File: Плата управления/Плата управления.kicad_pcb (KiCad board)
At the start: 2 copper layers, 66 x 58.4 mm, 113 parts, among them J1 Conn_01x10, J10 Conn_01x02, J11 Conn_01x03, J2 Conn_01x10, J3 Conn_01x02, J4 A, J5 B, J6 C, J7 Conn_01x02, J8 Conn_01x02, J9 Conn_01x02, U1 AT25xxx, U2 LMV7239M5, U3 LMV324, U4 STM32F767VITx, U5 INA283, Y1 8M

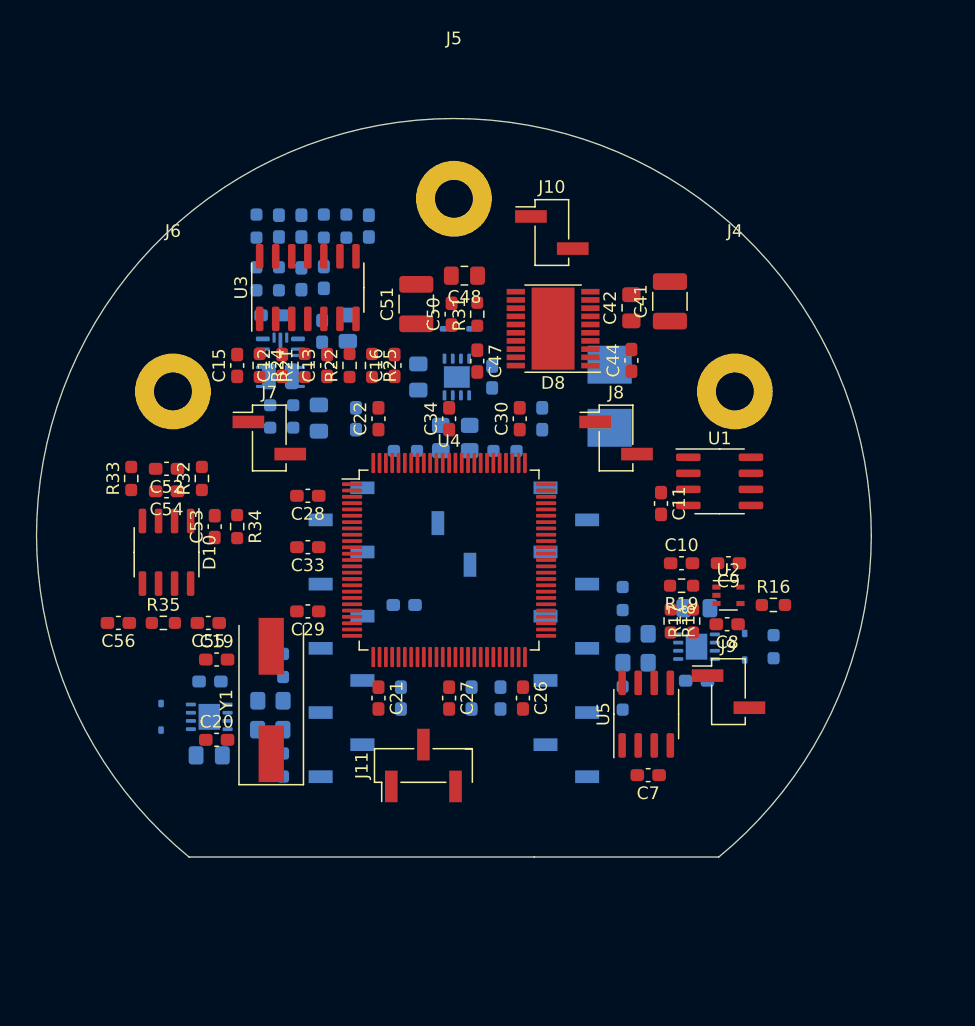
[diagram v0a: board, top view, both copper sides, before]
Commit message: Изменил контур под новую крышку
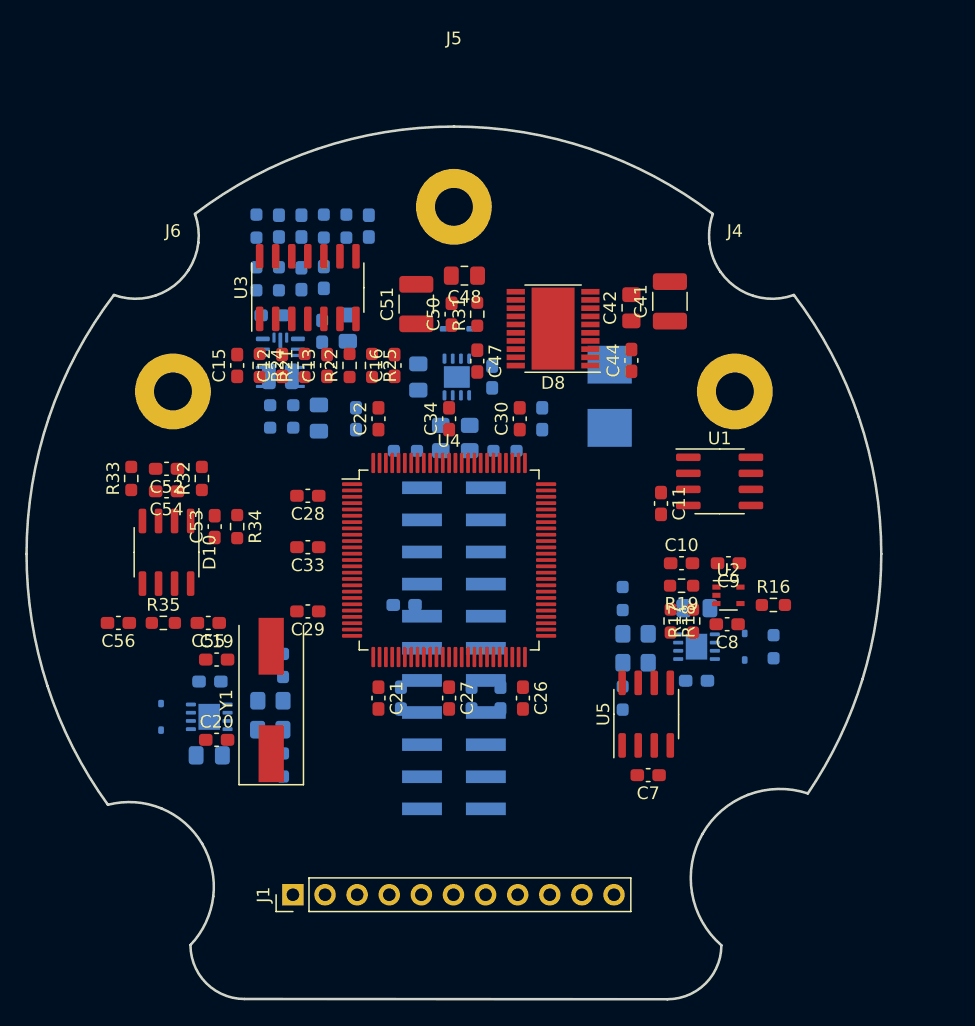
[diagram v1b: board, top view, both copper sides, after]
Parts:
- removed J10, J7, J8, J9: Conn_01x02, Connector_PinHeader_2.54mm:PinHeader_1x02_P2.54mm_Vertical_SMD_Pin1Left
- removed J11: Conn_01x03, Connector_PinHeader_2.54mm:PinHeader_1x03_P2.54mm_Vertical_SMD_Pin1Left
- removed J2: Conn_01x10, Connector_PinSocket_2.54mm:PinSocket_1x10_P2.54mm_Vertical_SMD_Pin1Right
- removed J3: Conn_01x02, Connector_PinSocket_2.54mm:PinSocket_1x02_P2.54mm_Vertical_SMD_Pin1Left
- added J12: Conn_02x11_Odd_Even, Connector_PinHeader_2.54mm:PinHeader_2x11_P2.54mm_Vertical_SMD, B.Cu at (83.2, 103.5)
- J1: value Conn_01x10 -> Conn_01x11; footprint Connector_PinSocket_2.54mm:PinSocket_1x10_P2.54mm_Vertical_SMD_Pin1Left -> Connector_PinHeader_2.54mm:PinHeader_1x11_P2.54mm_Vertical; moved to F.Cu
- moved J1 21.1 mm to (70.5, 123.0), turned to 90 degrees
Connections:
- J1 pad 1: Temp_B -> GND
- J1 pad 10: G5 -> GND
- J1 pad 2: GND -> Current_C_MCU
- J1 pad 4: G4 -> +3.3V
- J1 pad 5: GND -> SCLK_MCU
- J1 pad 6: G6 -> CS_MCU
- J1 pad 7: Temp_C -> SDIO_MCU
- J1 pad 9: C -> Current_B_MCU
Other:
- board size 66 x 58.4 mm -> 67.6 x 69 mm

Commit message: Добавил разъёмы под интерфейсы
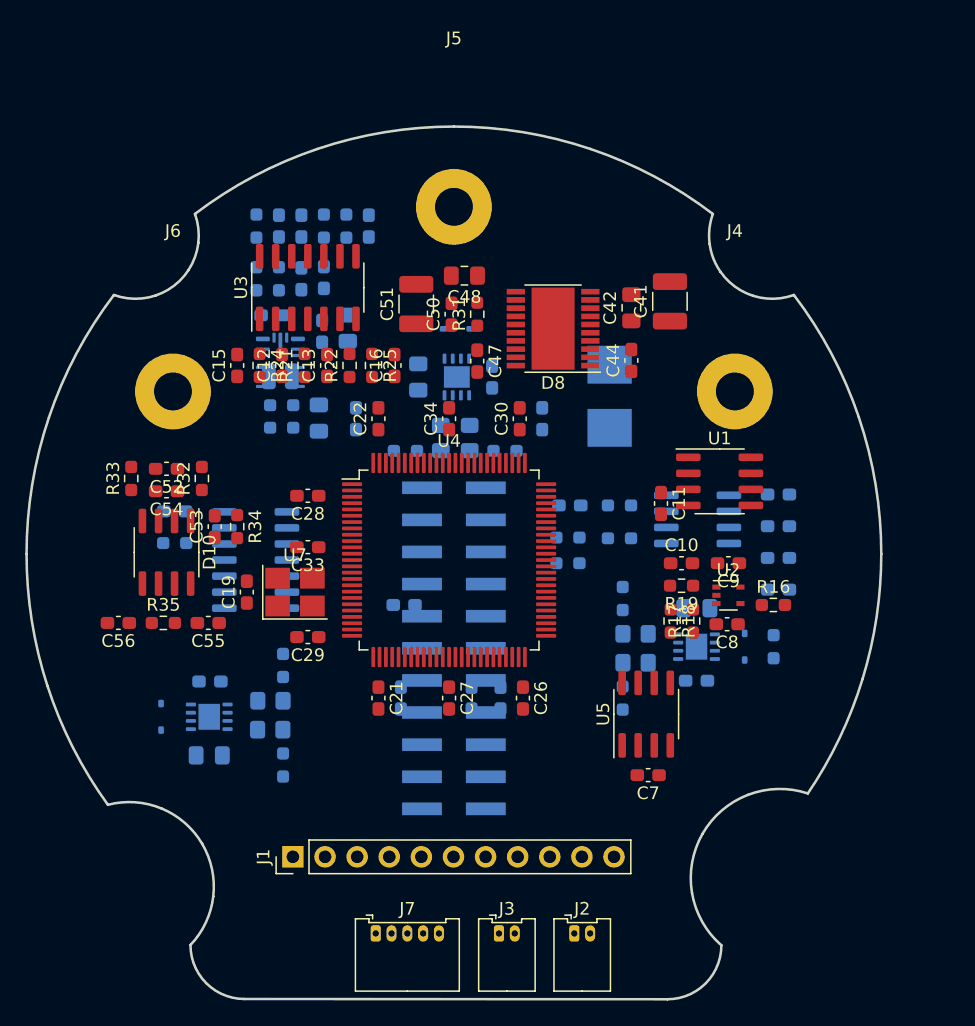
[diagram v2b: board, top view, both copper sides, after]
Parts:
- removed C20: 4.3p, Capacitor_SMD:C_0603_1608Metric_Pad1.08x0.95mm_HandSolder
- removed Y1: 8M, Crystal:Crystal_SMD_HC49-SD
- added C38: 1u, Capacitor_SMD:C_0603_1608Metric_Pad1.08x0.95mm_HandSolder, B.Cu at (108.9, 91.3)
- added C39: 56p, Capacitor_SMD:C_0603_1608Metric_Pad1.08x0.95mm_HandSolder, B.Cu at (108.9, 93.8)
- added C40: 1u, Capacitor_SMD:C_0603_1608Metric_Pad1.08x0.95mm_HandSolder, B.Cu at (108.9, 96.4)
- added C57: 56p, Capacitor_SMD:C_0603_1608Metric_Pad1.08x0.95mm_HandSolder, B.Cu at (108.9, 98.9)
- added C58: 56p, Capacitor_SMD:C_0603_1608Metric_Pad1.08x0.95mm_HandSolder, B.Cu at (92.4, 92.2)
- added C59: 0.1u, Capacitor_SMD:C_0603_1608Metric_Pad1.08x0.95mm_HandSolder, B.Cu at (61.1, 92.7)
- added D7: SIT65HVD232DR, Package_SO:SOIC-8_3.9x4.9mm_P1.27mm, B.Cu at (102.5, 93.3)
- added J2: CAN2, Connector_Molex:Molex_PicoBlade_53048-0210_1x02_P1.25mm_Horizontal, F.Cu at (92.7, 126.1)
- added J3: CAN1, Connector_Molex:Molex_PicoBlade_53048-0210_1x02_P1.25mm_Horizontal, F.Cu at (86.8, 126.1)
- added J7: RS485, Connector_Molex:Molex_PicoBlade_53048-0510_1x05_P1.25mm_Horizontal, F.Cu at (77.0, 126.1)
- added R27: 10k, Resistor_SMD:R_0603_1608Metric_Pad0.98x0.95mm_HandSolder, B.Cu at (96.3, 92.2)
- added R28: 10k, Resistor_SMD:R_0603_1608Metric_Pad0.98x0.95mm_HandSolder, B.Cu at (96.3, 94.8)
- added R36: 10k, Resistor_SMD:R_0603_1608Metric_Pad0.98x0.95mm_HandSolder, B.Cu at (92.2, 94.7)
- added R37: 120, Resistor_SMD:R_0603_1608Metric_Pad0.98x0.95mm_HandSolder, B.Cu at (92.2, 96.8)
- added R38: 120, Resistor_SMD:R_0603_1608Metric_Pad0.98x0.95mm_HandSolder, B.Cu at (61.1, 95.2)
- added U6: ADM3491ExR, Package_SO:SOIC-14_3.9x8.7mm_P1.27mm, B.Cu at (67.5, 96.5)
- added U7: ASEMB-10, Oscillator:Oscillator_SMD_Abracon_ASE-4Pin_3.2x2.5mm_HandSoldering, F.Cu at (70.6, 99.1)
- C19: value 4.3p -> 0.1u
- C52, C54: value 56p -> 1u
- moved C19 5.84 mm to (66.8, 99.1), turned to 90 degrees
- moved J1 3.00 mm to (70.5, 120.0)
- moved C29 2.03 mm to (71.6, 102.6)
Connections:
- net CANH renamed CAN1H
- net CANL renamed CAN1L
- net CAN_RXD renamed CAN1_RXD_MCU
- net CAN_TXD renamed CAN1_TXD_MCU
- C19 pad 2: Net-(U4-PH0) -> +3.3V
- U4 pad 13: Net-(U4-PH1) -> GND

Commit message: Новый контур платы
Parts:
- removed R34, R36: 10k, Resistor_SMD:R_0603_1608Metric_Pad0.98x0.95mm_HandSolder
- added C20: 56p, Capacitor_SMD:C_0603_1608Metric_Pad1.08x0.95mm_HandSolder, B.Cu at (105.7, 98.0)
- added C60: 56p, Capacitor_SMD:C_0603_1608Metric_Pad1.08x0.95mm_HandSolder, B.Cu at (108.2, 98.0)
- added C61: 56p, Capacitor_SMD:C_0603_1608Metric_Pad1.08x0.95mm_HandSolder, B.Cu at (103.6, 94.0)
- added J10: Conn_02x03_Odd_Even, Connector_PinHeader_2.54mm:PinHeader_2x03_P2.54mm_Vertical_SMD, F.Cu at (108.2, 99.1)
- added J8: Conn_02x03_Odd_Even, Connector_PinHeader_2.54mm:PinHeader_2x03_P2.54mm_Vertical_SMD, F.Cu at (65.0, 109.2)
- added R39: 120, Resistor_SMD:R_0603_1608Metric_Pad0.98x0.95mm_HandSolder, B.Cu at (105.7, 102.1)
- added R40: 120, Resistor_SMD:R_0603_1608Metric_Pad0.98x0.95mm_HandSolder, B.Cu at (108.2, 102.1)
- added R41: 120, Resistor_SMD:R_0603_1608Metric_Pad0.98x0.95mm_HandSolder, B.Cu at (105.7, 94.0)
- C12, C13, C55, C56, C7, C8, R16, R24, R25, U3, U5: moved to B.Cu
- C14, C17, C18, C23, C31, C32, C35, C36, C37, C38, C39, C40, C43, C45, C46, C49, C59, D7, D9, R27, R28, R29, R30, R37, R38, U6: moved to F.Cu
- J1: value Conn_01x11 -> RS485; footprint Connector_PinHeader_2.54mm:PinHeader_1x11_P2.54mm_Vertical -> Connector_Molex:Molex_PicoBlade_53048-0510_1x05_P1.25mm_Horizontal
- J12: value Conn_02x11_Odd_Even -> Power
- moved C37 37.1 mm to (55.9, 101.0)
- moved C56 37.0 mm to (84.8, 125.5), turned to 90 degrees
- moved R33 37.0 mm to (94.5, 93.7), turned to 180 degrees
- moved R20 36.1 mm to (55.9, 101.0), turned to -90 degrees
- moved C55 35.5 mm to (89.9, 125.5), turned to -90 degrees
- moved C53 35.1 mm to (91.4, 116.1)
- moved C54 35.1 mm to (87.6, 113.3)
- moved C52 35.1 mm to (87.6, 111.5)
- moved D10 35.1 mm to (87.6, 118.1)
- moved R35 35.0 mm to (87.6, 123.2)
- moved R38 34.9 mm to (81.3, 123.7), turned to 0 degrees
- moved R23 32.9 mm to (61.6, 101.0), turned to 90 degrees
- moved C14 32.3 mm to (61.6, 101.0), turned to 90 degrees
- moved R32 31.3 mm to (94.5, 91.9), turned to 180 degrees
- moved C17 31.3 mm to (64.1, 101.0), turned to 90 degrees
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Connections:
- net Current_C_MCU renamed Digital_input2
- net SCLK_MCU renamed Analog_Input1
- J1 pad 3: GND -> Digital_input1
- J1 pad 4: +3.3V -> Analog_Input2
- U4 pad 51: unconnected-(U4-PB12-Pad51) -> CAN2_RXD_MCU
- U4 pad 52: unconnected-(U4-PB13-Pad52) -> CAN2_TXD_MCU
- U4 pad 70: unconnected-(U4-PA11-Pad70) -> CAN1_RXD_MCU
- U4 pad 71: unconnected-(U4-PA12-Pad71) -> CAN1_TXD_MCU
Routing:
- net GND: track 0.00 -> 84.7 mm, vias 0 -> 17
- net +3.3V: track 0.00 -> 63.6 mm, vias 0 -> 3
- net +12V: track 0.00 -> 23.3 mm, vias 0 -> 1
- net VDDA: track 0.00 -> 22.6 mm
- net C: track 0.00 -> 13.2 mm, vias 0 -> 2
- net Net-(D8-L1): track 0.00 -> 12.8 mm, vias 0 -> 1
- net Temp_C: track 0.00 -> 9.45 mm, vias 0 -> 2
- net Net-(D8-L2): track 0.00 -> 9.36 mm, vias 0 -> 1
- net +24V: track 0.00 -> 9.00 mm, vias 0 -> 1
- net Temp_B: track 0.00 -> 7.42 mm, vias 0 -> 2
- net Temp_A: track 0.00 -> 7.10 mm, vias 0 -> 2
- net Net-(D8-VOS_FB): track 0.00 -> 6.78 mm
- net G6: track 0.00 -> 6.60 mm
- net G1: track 0.00 -> 6.60 mm
- net G2: track 0.00 -> 6.60 mm
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- added copper zone on B.Cu, net GND
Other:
- board size 67.6 x 69 mm -> 67 x 68.5 mm

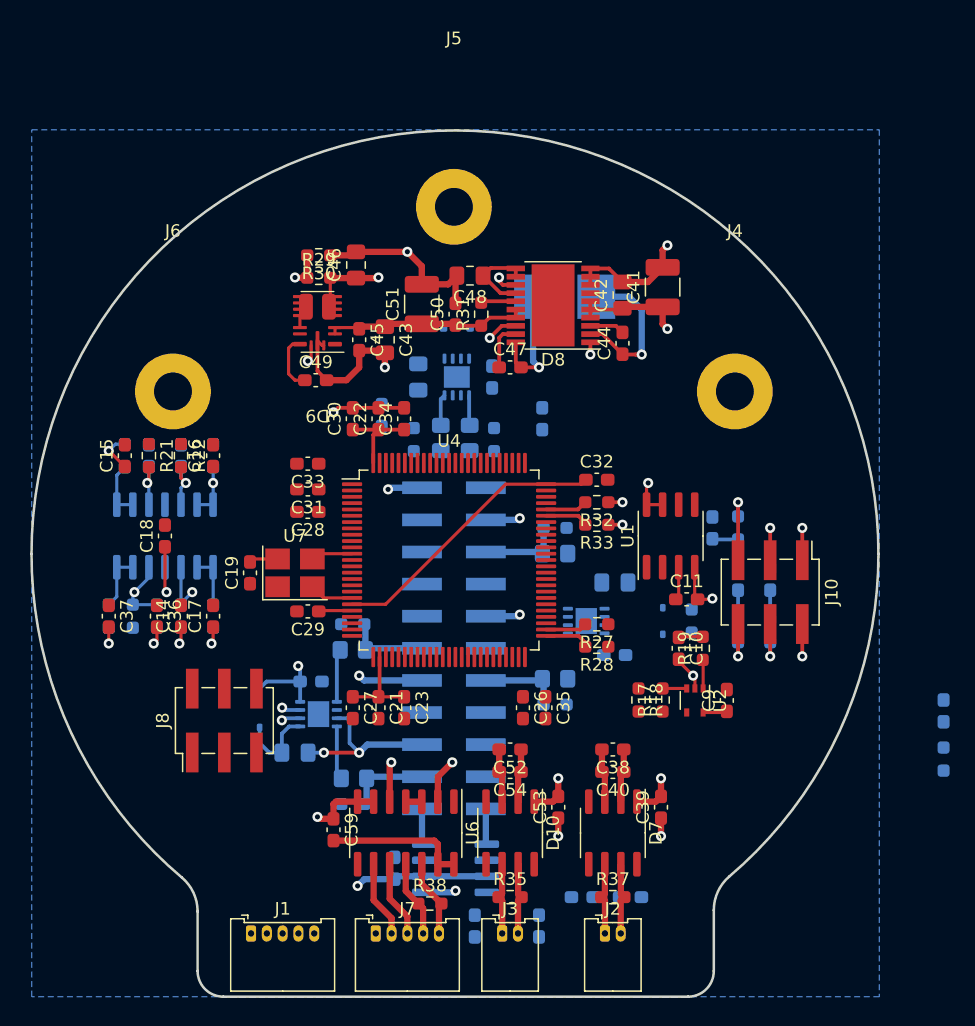
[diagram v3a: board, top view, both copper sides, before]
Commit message: Заменил разъём под силовую плату
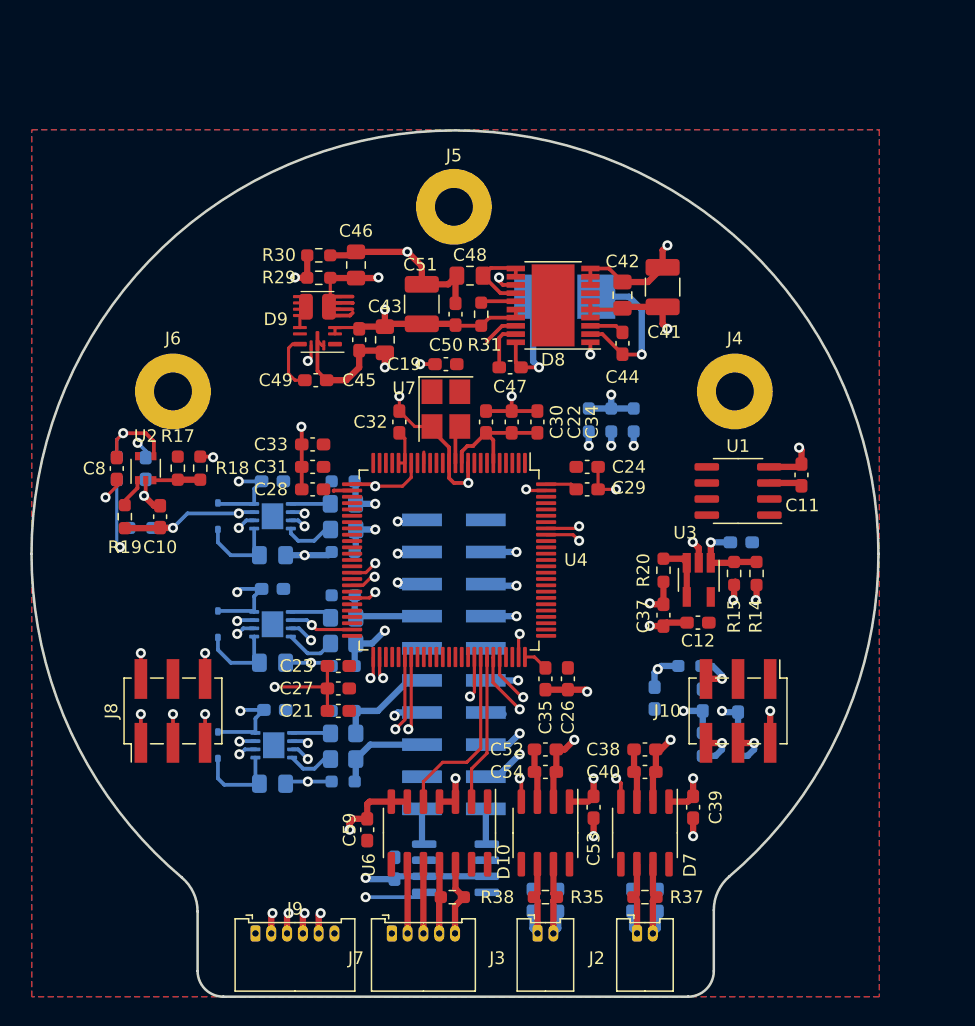
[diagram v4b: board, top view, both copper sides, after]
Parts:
- removed C13, C14, C18: 100n, Capacitor_SMD:C_0603_1608Metric_Pad1.08x0.95mm_HandSolder
- removed C15, C16, C17: 56p, Capacitor_SMD:C_0603_1608Metric_Pad1.08x0.95mm_HandSolder
- removed C25: 1u, Capacitor_SMD:C_0603_1608Metric_Pad1.08x0.95mm_HandSolder
- removed J12: Power, Connector_PinHeader_2.54mm:PinHeader_2x11_P2.54mm_Vertical_SMD
- removed R24, R25, R26: 120, Resistor_SMD:R_0603_1608Metric_Pad0.98x0.95mm_HandSolder
- removed R27, R28, R32, R33: 10k, Resistor_SMD:R_0603_1608Metric_Pad0.98x0.95mm_HandSolder
- added J9: Conn_01x06, Connector_Molex:Molex_PicoBlade_53048-0610_1x06_P1.25mm_Horizontal, F.Cu at (67.5, 126.1)
- C12, C24, C8, R14, R15, R20: moved to F.Cu
- C36, C9, R21, R22: moved to B.Cu
- J1: value RS485 -> Conn_02x10_Odd_Even; footprint Connector_Molex:Molex_PicoBlade_53048-0510_1x05_P1.25mm_Horizontal -> Connector_PinHeader_2.54mm:PinHeader_2x10_P2.54mm_Vertical_SMD; moved to B.Cu
- U3: value LMV324 -> LMV321; footprint Package_SO:SOIC-14_3.9x8.7mm_P1.27mm -> Package_TO_SOT_SMD:SOT-23-5_HandSoldering; moved to F.Cu
- moved R16 69.3 mm to (56.5, 89.3)
- moved C8 68.2 mm to (56.5, 89.3), turned to -90 degrees
- moved C9 49.5 mm to (58.8, 89.3), turned to -90 degrees
- moved R14 49.5 mm to (107.1, 97.6)
- moved U2 47.2 mm to (58.8, 89.3), turned to 90 degrees
- moved R19 46.9 mm to (57.1, 93.1), turned to -90 degrees
- moved C36 46.6 mm to (105.9, 95.1), turned to 0 degrees
- moved R15 45.8 mm to (105.3, 97.6)
- moved C12 45.4 mm to (102.5, 101.5), turned to 180 degrees
- moved R1 44.2 mm to (58.4, 94.0), turned to 0 degrees
- moved R20 44.0 mm to (99.8, 97.3)
- moved C37 43.9 mm to (99.8, 100.9)
- moved R17 42.5 mm to (61.3, 89.3), turned to -90 degrees
- moved U3 42.4 mm to (102.6, 98.1)
- moved C10 42.3 mm to (59.9, 93.1), turned to 90 degrees
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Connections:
- net SCK_MCCU renamed SCK_MCU
- C12 pad 1: GND -> +3.3V
- C12 pad 2: Temp_A -> GND
- C36 pad 1: Net-(U3D-+) -> Net-(U3-+)
- C39 pad 2: Net-(D7-D) -> CAN2_TXD_MCU
- C53 pad 2: Net-(D10-D) -> CAN1_TXD_MCU
- D10 pad 1: Net-(D10-D) -> CAN1_TXD_MCU
- D10 pad 4: Net-(D10-R) -> CAN1_RXD_MCU
- D7 pad 1: Net-(D7-D) -> CAN2_TXD_MCU
- D7 pad 4: Net-(D7-R) -> CAN2_RXD_MCU
- J1 pad 1: GND -> +3.3V
- J1 pad 2: Digital_input2 -> ~{OS}_MCU
- J1 pad 3: Digital_input1 -> G3
- J1 pad 4: Analog_Input2 -> SCL_MCU
- J1 pad 5: Analog_Input1 -> B
- J4 pad 1: A -> unconnected-(J4-Pin_1-Pad1)
- J5 pad 1: B -> unconnected-(J5-Pin_1-Pad1)
- J6 pad 1: C -> unconnected-(J6-Pin_1-Pad1)
- R14 pad 2: Net-(U3D-+) -> Net-(U3-+)
- R15 pad 1: Net-(U3D-+) -> Net-(U3-+)
- R20 pad 1: Net-(U3D--) -> Net-(U3--)
- R21 pad 1: +3.3V -> SDA_MCU
- R21 pad 2: Temp_A -> +3.3V
- R22 pad 1: +3.3V -> SCL_MCU
- R22 pad 2: Temp_B -> +3.3V
- R23 pad 1: +3.3V -> ~{OS}_MCU
- R23 pad 2: Temp_C -> +3.3V
- U3 pad 1: Net-(U3A--) -> Net-(U3-+)
- U3 pad 2: Net-(U3A--) -> GND
- U3 pad 3: Temp_A -> Net-(U3--)
- U3 pad 4: +3.3V -> Net-(U3--)
- U3 pad 5: Temp_B -> +3.3V
- U4 pad 21: +3.3V -> VDDA
- U4 pad 40: unconnected-(U4-PE10-Pad40) -> IN_A
- U4 pad 42: unconnected-(U4-PE12-Pad42) -> IN_B
- U4 pad 44: unconnected-(U4-PE14-Pad44) -> IN_C
- U4 pad 51: CAN2_RXD_MCU -> CAN1_RXD_MCU
- U4 pad 52: CAN2_TXD_MCU -> CAN1_TXD_MCU
- U4 pad 56: unconnected-(U4-PD9-Pad56) -> Digital_input2
- U4 pad 57: unconnected-(U4-PD10-Pad57) -> Digital_input1
- U4 pad 67: unconnected-(U4-PA8-Pad67) -> RS_485_Enable_MCU
- U4 pad 68: unconnected-(U4-PA9-Pad68) -> TX_MCU
- U4 pad 69: unconnected-(U4-PA10-Pad69) -> RX_MCU
- U4 pad 70: CAN1_RXD_MCU -> CAN2_RXD_MCU
- U4 pad 71: CAN1_TXD_MCU -> CAN2_TXD_MCU
- U4 pad 75: VDDA -> +3.3V
- U4 pad 92: unconnected-(U4-PB6-Pad92) -> SCL_MCU
- U4 pad 93: unconnected-(U4-PB7-Pad93) -> SDA_MCU
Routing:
- net GND: track 84.7 -> 141.5 mm, vias 17 -> 34
- net Net-(R16-Pad2): track 2.53 -> 45.9 mm, vias 1 -> 2
- net Enable: track 3.43 -> 39.2 mm, vias 1 -> 4
- net Digital_input2: track 0.00 -> 27.3 mm, vias 0 -> 2
- net Digital_input1: track 0.00 -> 27.2 mm, vias 0 -> 2
- net B: track 2.73 -> 28.6 mm, vias 1 -> 3
- net IN_C: track 1.52 -> 24.3 mm, vias 1 -> 2
- net CAN1_TXD_MCU: track 3.33 -> 24.9 mm, vias 0 -> 2
- net G3: track 0.00 -> 21.0 mm, vias 0 -> 2
- net CAN2_TXD_MCU: track 3.27 -> 23.6 mm, vias 0 -> 2
- net VDDA: track 22.6 -> 3.07 mm
- net G1: track 6.60 -> 23.6 mm, vias 0 -> 2
- net IN_B: track 0.00 -> 16.3 mm, vias 0 -> 2
- net IN_A: track 0.00 -> 15.8 mm, vias 0 -> 2
- net G2: track 6.60 -> 21.7 mm, vias 0 -> 2
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- added copper zone on In1.Cu, net +12V
- added copper zone on In1.Cu, net +24V
- added copper zone on F.Cu, net +3.3V
- added copper zone on In3.Cu, net +3.3V
- added copper zone on In3.Cu, net Enable
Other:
- copper layers 2 -> 6
